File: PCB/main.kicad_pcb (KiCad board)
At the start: 2 copper layers, 39 parts, among them CON1 BARREL_JACK, P1 JUMPER_LEFT, P2 LEFT, P3 JUMPER_RIGHT, P4 RIGHT, Q1 3904, Q2 3904, Q3 3904, Q4 3904, SW1 SW_PUSH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

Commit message: layout
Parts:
- moved C1 127.8 mm to (74.9, 20.3), turned to 270 degrees
- moved P4 119.1 mm to (144.8, 25.4)
- moved R13 111.9 mm to (134.6, 25.4), turned to 180 degrees
- moved P1 109.8 mm to (119.4, 48.3)
- moved R3 108.7 mm to (91.4, 33.0)
- moved R12 107.4 mm to (124.5, 27.9), turned to 180 degrees
- moved R4 106.1 mm to (99.1, 38.1), turned to 180 degrees
- moved R7 105.4 mm to (102.9, 24.1)
- moved R1 103.4 mm to (91.4, 17.8)
- moved R5 102.5 mm to (91.4, 48.3)
- moved R2 101.6 mm to (99.1, 22.9), turned to 180 degrees
- moved D1 98.0 mm to (110.5, 19.1), turned to 180 degrees
- moved P3 93.7 mm to (119.4, 19.1)
- moved Q4 91.2 mm to (130.8, 21.6), turned to 270 degrees
- moved D2 89.5 mm to (110.5, 34.3), turned to 180 degrees
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
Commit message: before traces
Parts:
- moved P2 61.6 mm to (144.8, 71.1)
- moved D4 52.2 mm to (137.2, 66.0), turned to 90 degrees
- moved R10 42.1 mm to (116.8, 68.6)
- moved R11 29.0 mm to (127.0, 66.0)
- moved C5 20.3 mm to (74.9, 71.1)
- moved Q1 19.8 mm to (125.7, 62.2)
- moved SW1 19.1 mm to (63.5, 40.6)
- moved C1 19.0 mm to (74.9, 39.4)
- moved CON1 18.9 mm to (64.8, 29.2)
- moved C3 17.8 mm to (74.9, 53.3)
- moved SW2 17.8 mm to (63.5, 54.6)
- moved SW3 16.5 mm to (63.5, 68.6)
- moved Q2 12.7 mm to (130.8, 62.2), turned to 270 degrees
- moved R9 11.4 mm to (102.9, 66.0)
- moved C6 11.4 mm to (104.1, 59.7)
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
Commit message: traces again
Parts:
- moved R13 7.62 mm to (127.0, 34.3), turned to 0 degrees
- moved C1 1.27 mm to (74.9, 38.1)
- moved C3 0.63 mm to (74.9, 54.0)
- moved D1 0.63 mm to (110.5, 28.6)
- moved D4 0.63 mm to (137.8, 66.0)
- moved D5 0.63 mm to (137.8, 34.3)
- turned SW3 to 0 degrees
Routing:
- net GND: track 0.00 -> 334.0 mm
- net Net-(CON1-Pad1): track 0.00 -> 85.3 mm
- net +3V3: track 0.00 -> 79.5 mm
- net +12V: track 0.00 -> 79.2 mm
- net +5V: track 0.00 -> 72.7 mm
- net Net-(P3-Pad2): track 0.00 -> 39.9 mm
- net Net-(P1-Pad2): track 0.00 -> 35.5 mm
- net Net-(C3-Pad1): track 0.00 -> 23.0 mm
- net Net-(C1-Pad1): track 0.00 -> 22.8 mm
- net Net-(C5-Pad1): track 0.00 -> 20.7 mm
- net Net-(Q1-Pad1): track 0.00 -> 20.2 mm
- net Net-(R5-Pad2): track 0.00 -> 19.4 mm
- net Net-(R3-Pad2): track 0.00 -> 19.4 mm
- net Net-(R1-Pad2): track 0.00 -> 19.4 mm
- net Net-(D5-Pad2): track 0.00 -> 16.5 mm
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
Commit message: edge cuts and oshpark settings
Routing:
- net Net-(CON1-Pad1): track 85.3 -> 45.7 mm
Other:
- board outline added: 96.5 x 58.4 mm
- net class Default: clearance 0.2 -> 0.1524; trace_width 0.25 -> 0.1524; via_dia 0.6 -> 0.6858; via_drill 0.4 -> 0.3302
- rule trace_clearance: 0.2 -> 0.1524
- rule trace_min: 0.2 -> 0.1524
- rule via_min_drill: 0.3 -> 0.3302
- rule via_min_size: 0.4 -> 0.6858

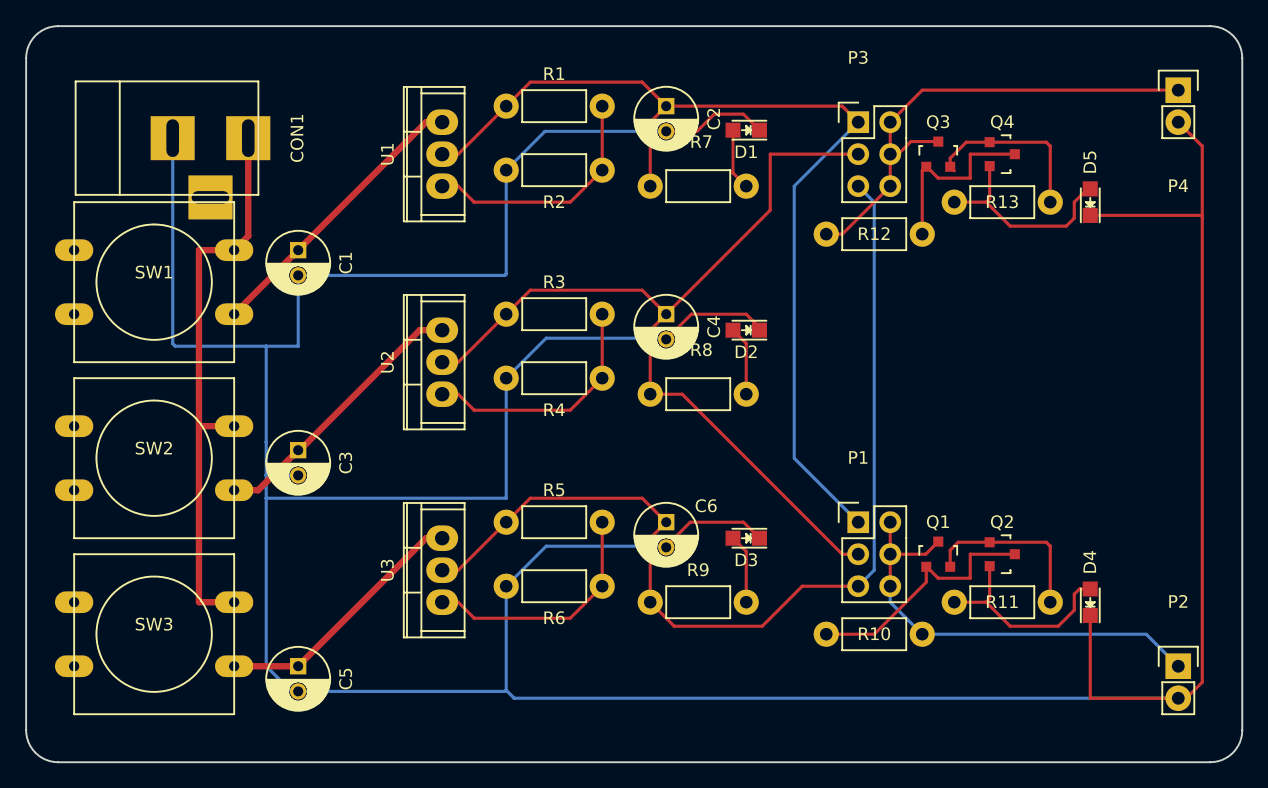
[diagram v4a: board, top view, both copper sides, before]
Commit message: real switches and oshpark test
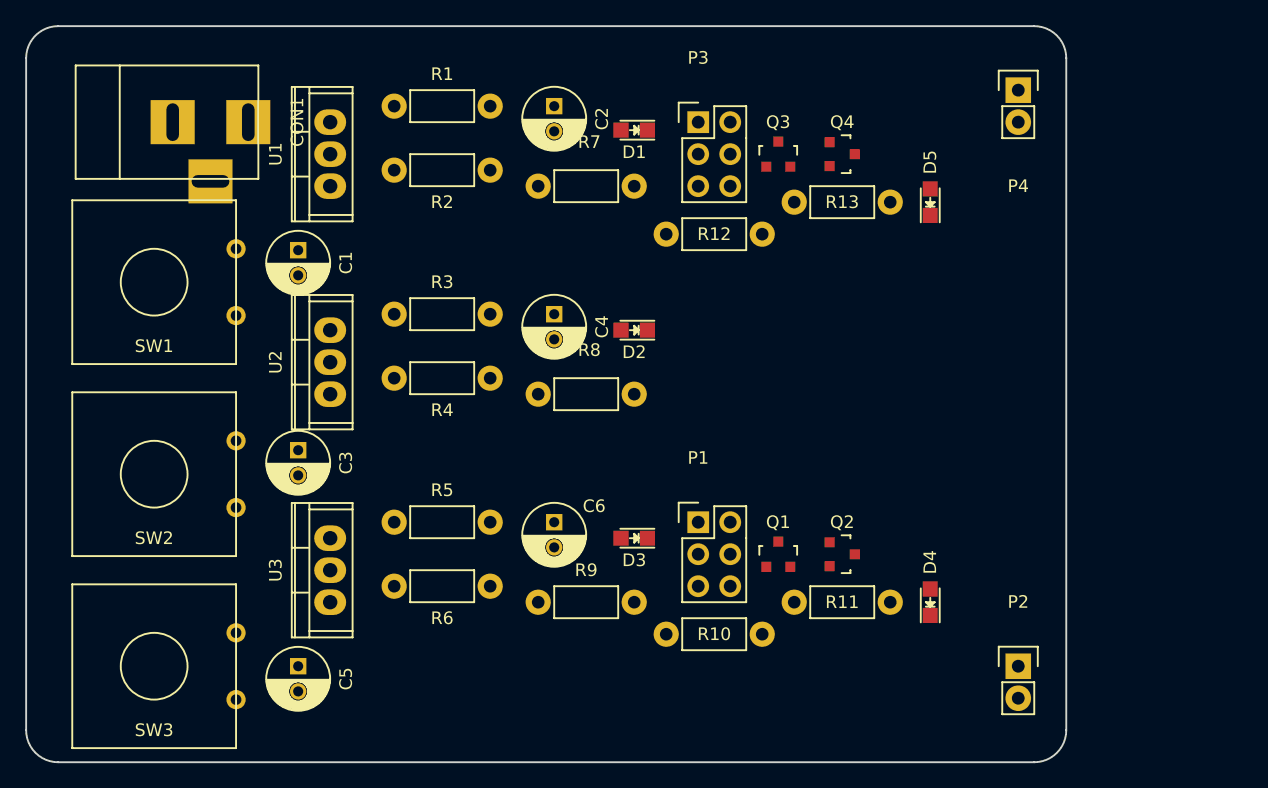
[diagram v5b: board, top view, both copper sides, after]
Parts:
- SW1, SW2, SW3: value SW_PUSH -> 12x12_PUSHBUTTON_SPST; footprint Buttons_Switches_ThroughHole:SW_PUSH-12mm -> myparts:12x12_PUSHBUTTON_SPST
- moved Q1 12.7 mm to (113.0, 62.2)
- moved Q2 12.7 mm to (118.1, 62.2)
- moved Q3 12.7 mm to (113.0, 30.5)
- moved Q4 12.7 mm to (118.1, 30.5)
- moved R10 12.7 mm to (104.1, 68.6)
- moved R11 12.7 mm to (114.3, 66.0)
- moved R13 12.7 mm to (114.3, 34.3)
- moved D4 12.7 mm to (125.1, 66.0)
- moved D5 12.7 mm to (125.1, 34.3)
- moved P1 12.7 mm to (106.7, 59.7)
- moved P2 12.7 mm to (132.1, 71.1)
- moved P3 12.7 mm to (106.7, 27.9)
- moved P4 12.7 mm to (132.1, 25.4)
- moved R12 12.7 mm to (111.8, 36.8)
- moved C2 8.89 mm to (95.2, 26.7)
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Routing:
- net GND: track 334.0 -> 0.00 mm
- net +3V3: track 79.5 -> 0.00 mm
- net +12V: track 79.2 -> 0.00 mm
- net +5V: track 72.7 -> 0.00 mm
- net Net-(CON1-Pad1): track 45.7 -> 0.00 mm
- net Net-(P3-Pad2): track 39.9 -> 0.00 mm
- net Net-(P1-Pad2): track 35.5 -> 0.00 mm
- net Net-(C3-Pad1): track 23.0 -> 0.00 mm
- net Net-(C1-Pad1): track 22.8 -> 0.00 mm
- net Net-(C5-Pad1): track 20.7 -> 0.00 mm
- net Net-(Q1-Pad1): track 20.2 -> 0.00 mm
- net Net-(R5-Pad2): track 19.4 -> 0.00 mm
- net Net-(R3-Pad2): track 19.4 -> 0.00 mm
- net Net-(R1-Pad2): track 19.4 -> 0.00 mm
- net Net-(D5-Pad2): track 16.5 -> 0.00 mm
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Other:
- board size 96.5 x 58.4 mm -> 82.5 x 58.4 mm
